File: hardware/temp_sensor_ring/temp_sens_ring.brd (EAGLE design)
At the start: 19 x 20 mm, 14 parts, among them IC1 MCP9808

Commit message: PCB completed, part library created
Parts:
- moved R1 0.16 mm to (7.09, 13.6)
- moved J3 0.05 mm to (7.02, 8.10)
- turned R2 to 0 degrees
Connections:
- net GND: now also R2.P$1, R2.P$2, R2.P$3, R2.P$4; no longer R2.P$5, R2.P$6, R2.P$7, R2.P$8
- net N$1: now also R2.P$7; no longer R2.P$3
- net N$2: now also R2.P$6; no longer R2.P$2
- net N$3: now also R2.P$5; no longer R2.P$1
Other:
- board text added: "0"
- board text added: "1"
- board text added: "2"
- board text added: "3"
- board text added: "4"
- board text added: "A.JENERTS"
- board text added: "A0"
- board text added: "A1"
- board text added: "A2"
- board text added: "Oct. 2021"

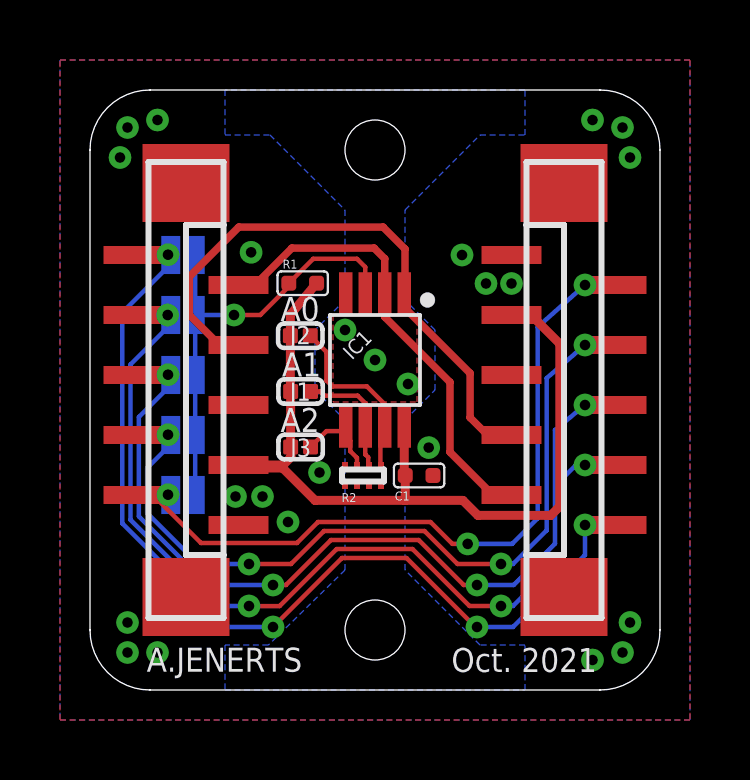
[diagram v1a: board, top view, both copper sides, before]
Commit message: 3D models added to library
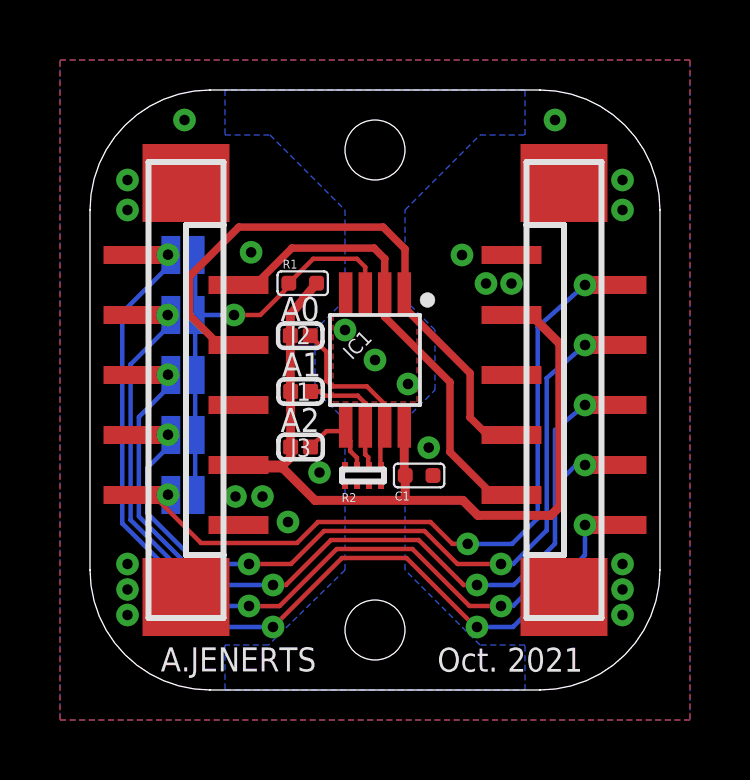
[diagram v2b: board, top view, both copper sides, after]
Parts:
- C1: device SIG_Parts:0402 -> temp_sens_ring:C0402
- IC1: device SIG_Parts:MSOP-8 -> temp_sens_ring:MSOP-8
- J1, J2, J3: device SIG_Parts:SMT_JUMP_2_NO_SMALL -> temp_sens_ring:SMT_JUMP_2_NO_SMALL
- JP4, JP5, JP6, JP7, JP8: device SparkFun-Jumpers:SMT-JUMPER_2_NO_NO-SILK -> temp_sens_ring:SMT-JUMPER_2_NO_NO-SILK
- R1: device SIG_Parts:0402 -> temp_sens_ring:0402
- R2: device SIG_Parts:R0502_4X -> temp_sens_ring:R0502_4X
- X1, X2: device SIG_Parts:FFC_1X10_VERTICAL -> temp_sens_ring:FFC_1X10_VERTICAL
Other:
- outline, holes or cut-outs redrawn
